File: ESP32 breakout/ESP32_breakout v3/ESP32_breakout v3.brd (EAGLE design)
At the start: 99.1 x 76.2 mm, 54 parts, among them J3 SCHA4B0419, Q3 BSS84, U1 ESP-WROOM-32, U2 NCP-1117223-3, U3 MCP2221ATSSOP14

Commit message: Layout and 80% routing done
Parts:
- removed R13: 10k, dr-library:RES-0603
- removed S1, S2: (no value), dr-library:SKHMQME010
- added BOOT, RST: (no value), dr-library:SKHMQME010
- added JP7, JP8: JUMPER_2-WAY, dr-library:1X02
- added R3: 10k, dr-library:RES-0603
- moved R12 83.8 mm to (7.62, 7.62), turned to 180 degrees
- moved R10 80.1 mm to (7.62, 10.2), turned to 180 degrees
- moved R9 80.1 mm to (11.4, 8.89), turned to 180 degrees
- moved C19 77.5 mm to (7.62, 12.7), turned to 180 degrees
- moved R14 76.3 mm to (7.62, 5.08), turned to 180 degrees
- moved R11 72.6 mm to (11.4, 11.4)
- moved J3 62.5 mm to (19.1, 22.9), turned to 270 degrees
- moved Q3 39.2 mm to (52.7, 29.2)
- moved R16 38.9 mm to (38.7, 29.2), turned to 270 degrees
- moved R8 37.6 mm to (57.1, 29.2), turned to 90 degrees
- moved R7 36.5 mm to (48.3, 29.2), turned to 270 degrees
- moved D7 36.4 mm to (38.7, 39.4), turned to 90 degrees
- moved R6 35.3 mm to (41.9, 29.2), turned to 270 degrees
- moved D5 32.4 mm to (41.9, 39.4), turned to 90 degrees
- moved R5 31.9 mm to (45.1, 29.2), turned to 270 degrees
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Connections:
- new net N$1: JP7.1, R9.1
- new net N$6: JP8.1, R3.1
- net +3V3: now also JP7.2, JP8.2; no longer R13.1, R9.1
- net CLK: no longer J3.5, R12.2
- net CMD: no longer J3.3, R11.2
- net EN: now also RST.3, RST.4; no longer S1.3, S1.4
- net GND: now also BOOT.1, BOOT.2, RST.1, RST.2; no longer S1.1, S1.2, S2.1, S2.2
- net IO0/T1: now also BOOT.3, BOOT.4; no longer S2.3, S2.4
- net IO12/T5: now also J3.1, R9.2
- net IO13/T4: now also J3.2, R10.2
- net IO14/T6: now also J3.5, R12.2
- net IO15/T3: now also J3.3, R11.2
- net IO2/T2: now also J3.7, R3.2
- net IO4/T0: now also J3.8, R14.2
- net SD0: no longer J3.7, R13.2
- net SD1: no longer J3.8, R14.2
- net SD2: no longer J3.1, R9.2
- net SD3: no longer J3.2, R10.2
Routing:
- net IO12/T5: track 0.00 -> 181.3 mm, vias 0 -> 5
- net IO14/T6: track 0.00 -> 180.7 mm, vias 0 -> 3
- net IO2/T2: track 0.00 -> 178.0 mm, vias 0 -> 3
- net IO15/T3: track 0.00 -> 153.0 mm, vias 0 -> 3
- net IO4/T0: track 0.00 -> 149.3 mm
- net IO13/T4: track 0.00 -> 140.4 mm, vias 0 -> 3
- net EN: track 0.00 -> 105.6 mm, vias 0 -> 1
- net IO0/T1: track 0.00 -> 102.0 mm, vias 0 -> 1
- net S_VP: track 0.00 -> 82.4 mm, vias 0 -> 1
- net S_VN: track 0.00 -> 80.0 mm, vias 0 -> 1
- net IO34: track 0.00 -> 72.2 mm, vias 0 -> 1
- net IO27/T7: track 0.00 -> 70.6 mm, vias 0 -> 1
- net IO35: track 0.00 -> 70.2 mm, vias 0 -> 1
- net IO19: track 0.00 -> 63.4 mm, vias 0 -> 2
- net +3V3: track 0.00 -> 63.2 mm, vias 0 -> 3
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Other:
- board size 99.1 x 76.2 mm -> 95.2 x 76.2 mm
- board text added: "NOTES Buttons further apart microSD should be more isolated microSD pinout HS2_CMD - io15 HS2_CLK - io14 HS2_D0 - io2 HS2_D1 - io4 HS2_D2 - io12 HS2_D3 - io13"

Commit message: v3 routing
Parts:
- added JP10, JP9: M02LONG, dr-library:1X02-LONG
- moved JP5 2.84 mm to (47.0, 5.08), turned to 270 degrees
- moved JP4 1.80 mm to (35.6, 5.08), turned to 270 degrees
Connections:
- net +3V3: now also JP10.2
- net GND: now also JP10.1, JP9.1
- net VCC: now also JP9.2
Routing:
- net +3V3: track 63.2 -> 389.0 mm, vias 3 -> 7
- net GND: track 26.6 -> 166.9 mm, vias 0 -> 54
- net VCC: track 0.00 -> 100.4 mm, vias 0 -> 1
- net IO0/T1: track 102.0 -> 160.0 mm, vias 1 -> 3
- net RX: track 17.9 -> 75.5 mm, vias 0 -> 3
- net TX: track 13.6 -> 68.9 mm, vias 0 -> 3
- net EN: track 105.6 -> 139.5 mm, vias 1 -> 2
- net N$3: track 0.00 -> 16.1 mm, vias 0 -> 2
- net N$2: track 0.00 -> 6.56 mm
- net IO12/T5: track 181.3 -> 180.2 mm
- net USBCFG: track 48.9 -> 48.1 mm
- added copper zone on layer 1, net +3V3
- added copper zone on layer 1, net GND
- added copper zone on layer 16, net GND
- added copper zone on layer 1, net VCC

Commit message: Finished tracing part 2
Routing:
- net SD1: track 23.2 -> 22.3 mm
- net SD3: track 28.3 -> 27.4 mm
- net CMD: track 30.1 -> 29.2 mm
- net SD0: track 27.5 -> 26.6 mm
- net CLK: track 25.7 -> 24.8 mm
- net +3V3: vias 7 -> 8
- net VCC: vias 1 -> 2
- net GND: vias 54 -> 121
- added copper zone on layer 16, net +3V3
- added copper zone on layer 16, net VCC

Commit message: PCB made
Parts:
- removed D7: (no value), dr-library:LED-1206
- removed R16: 330, dr-library:RES-0603
- added D1: VS-10BQ030-M3, dr-library:DO-214AA
- added R13: 10k, dr-library:RES-0603
- D2: value VS-10BQ030-M3 -> (none); device dr-library:DO-214AA -> dr-library:LED-1206
- JP10, JP9: value M02LONG -> JUMPER_3-WAY; device dr-library:1X02-LONG -> dr-library:1X03
- JP6, JP7: value JUMPER_2-WAY -> M02LONG; device dr-library:1X02 -> dr-library:1X02-LONG
- R9: value 10k -> 330
- moved R3 71.3 mm to (80.6, 23.5), turned to 0 degrees
- moved R15 71.2 mm to (11.4, 6.35), turned to 180 degrees
- moved JP8 51.2 mm to (63.5, 27.9)
- moved R9 42.1 mm to (48.3, 29.2), turned to 270 degrees
- moved JP6 36.1 mm to (35.6, 5.08), turned to 90 degrees
- moved JP7 31.4 mm to (47.0, 5.08), turned to 90 degrees
- moved JP10 30.9 mm to (20.3, 10.2)
- moved JP9 24.7 mm to (15.2, 10.2)
- moved D2 20.3 mm to (35.6, 39.4), turned to 90 degrees
- moved D3 9.52 mm to (45.1, 39.4)
- moved R7 9.52 mm to (38.7, 29.2)
- moved R14 5.39 mm to (11.4, 8.89)
- moved JP4 3.81 mm to (39.4, 5.08), turned to 90 degrees
- moved JP5 3.81 mm to (50.8, 5.08), turned to 90 degrees
- moved D4 3.18 mm to (41.9, 39.4)
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- renumbered C18 to C8, C19 to C9, RST to RESET
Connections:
- removed net N$1: JP7.1, R9.1
- new net N$7: JP10.1, R15.1
- net +3V3: now also JP9.2, R13.1; no longer JP8.2, R14.1
- net GND: now also D2.C, JP6.1, JP7.1; no longer D7.C, JP10.1, JP9.1
- net HEART: now also JP8.1; no longer JP6.1
- net IO12/T5: now also R14.2; no longer R9.2
- net IO19: now also JP8.2; no longer JP6.2
- net IO2/T2: now also R15.2; no longer R3.2
- net IO4/T0: now also R13.2; no longer R14.2
- net N$10: now also R9.2; no longer R7.2
- net N$11: now also D4.A; no longer D5.A
- net N$2: now also D1.A; no longer D2.A
- net N$3: now also R3.1; no longer R15.1
- net N$4: now also D5.A, R7.1; no longer D7.A, R16.1
- net N$5: now also D2.A; no longer D3.A
- net N$6: now also JP9.1, R14.1; no longer JP8.1, R3.1
- net N$8: now also D3.A; no longer D4.A
- net N$9: now also R9.1; no longer R7.1
- net USBCFG: now also R7.2; no longer R16.2
- net VCC: now also D1.C, JP6.2; no longer D2.C, JP9.2
- net V_MCP: now also R3.2; no longer R15.2
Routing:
- net +3V3: track 389.0 -> 372.5 mm, vias 8 -> 23
- net N$7: track 0.00 -> 10.2 mm
- net N$1: track 6.09 -> 0.00 mm
- net GND: track 166.9 -> 163.1 mm, vias 121 -> 176
- net VCC: track 100.4 -> 97.5 mm, vias 2 -> 19
- net TX: track 68.9 -> 66.8 mm
- net RX: track 75.5 -> 73.3 mm
- net IO0/T1: track 160.0 -> 157.8 mm
- net IO19: track 63.4 -> 61.6 mm
- net SD1: track 22.3 -> 21.0 mm
- net CLK: track 24.8 -> 23.6 mm
- net S_VP: track 82.0 -> 80.7 mm
- net SD3: track 27.4 -> 26.1 mm
- net IO35: track 69.8 -> 68.5 mm
- net IO34: track 71.8 -> 70.6 mm
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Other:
- outline, holes or cut-outs redrawn
- board text added: "3.3V"
- board text added: "5V"
- board text added: "CLK"
- board text added: "CMD"
- board text added: "EN"
- board text added: "ESP32 Breakout D. Rances 10 Sep 2017 v3"
- board text added: "ESP32 Breakout and Development Board"
- board text added: "GND"
- board text added: "HEART"
- board text added: "HEART/IO19"
- board text added: "IO0"
- board text added: "IO12"
- board text added: "IO13"
- board text added: "IO14"
- board text added: "IO15"
- board text added: "IO16"
- board text added: "IO17"
- board text added: "IO18"
- board text added: "IO19"
- board text added: "IO2"
- board text added: "IO21"
- board text added: "IO22"
- board text added: "IO23"
- board text added: "IO25"
- board text added: "IO26"
- board text added: "IO27"
- board text added: "IO34"
- board text added: "IO35"
- board text added: "IO4"
- board text added: "IO5"
- board text added: "Pullups for DAT0 and DAT2 of microSD. Keep disabled to flash the ESP32"
- board text added: "RX"
- board text added: "Remove header to disconnect HEART LED and IO19"
- board text added: "SD0"
- board text added: "SD1"
- board text added: "SD2"
- board text added: "SD3"
- board text added: "SVN"
- board text added: "SVP"
- board text added: "Switch to enable USB-UART flashing and debugging"
- board text added: "T0"
- board text added: "T0/IO4"
- board text added: "T1"
- board text added: "T1/IO0"
- board text added: "T2"
- board text added: "T2/IO2"
- board text added: "T3"
- board text added: "T3/IO15"
- board text added: "T4"
- board text added: "T4/IO13"
- board text added: "T5"
- board text added: "T5/IO12"
- board text added: "T6"
- board text added: "T6/IO14"
- board text added: "T7"
- board text added: "T7/IO27"
- board text added: "TX"
- board text added: "USBCFG"
- board text added: "pullups disabled"
- board text added: "pullups enabled"
- board text removed: "NOTES Buttons further apart microSD should be more isolated microSD pinout HS2_CMD - io15 HS2_CLK - io14 HS2_D0 - io2 HS2_D1 - io4 HS2_D2 - io12 HS2_D3 - io13"

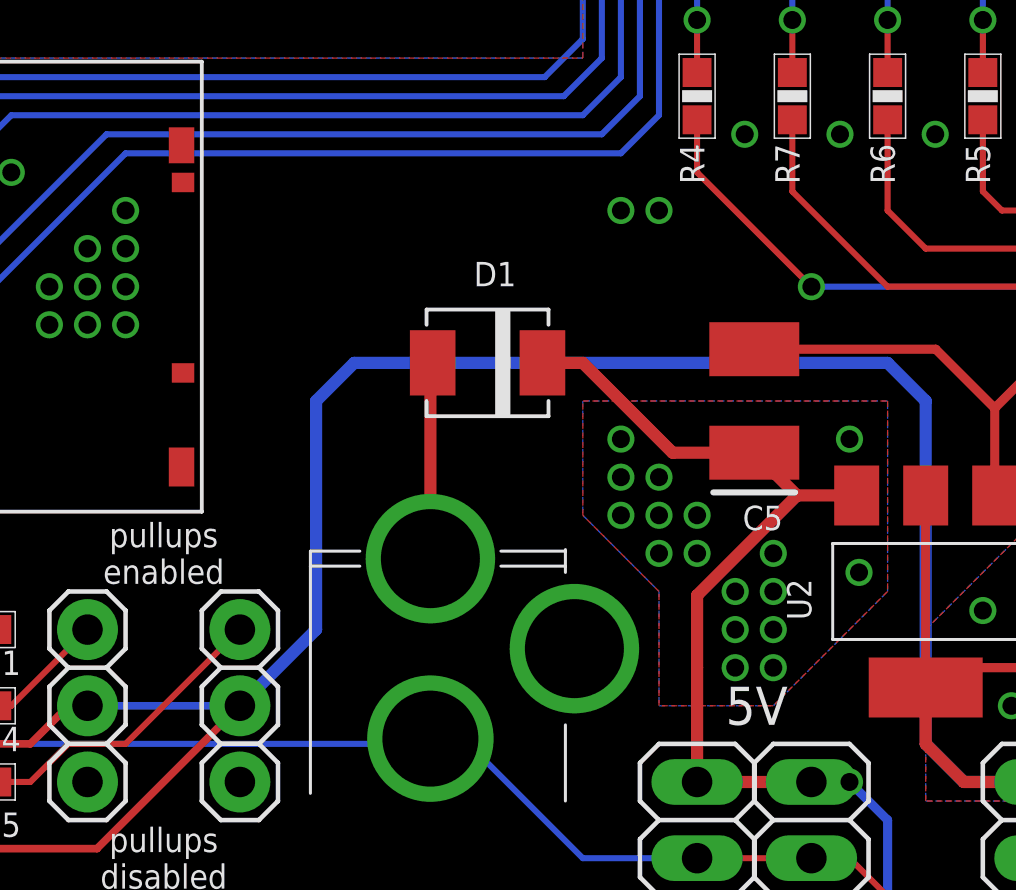
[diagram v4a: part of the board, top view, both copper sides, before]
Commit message: Added LED for microSD CD
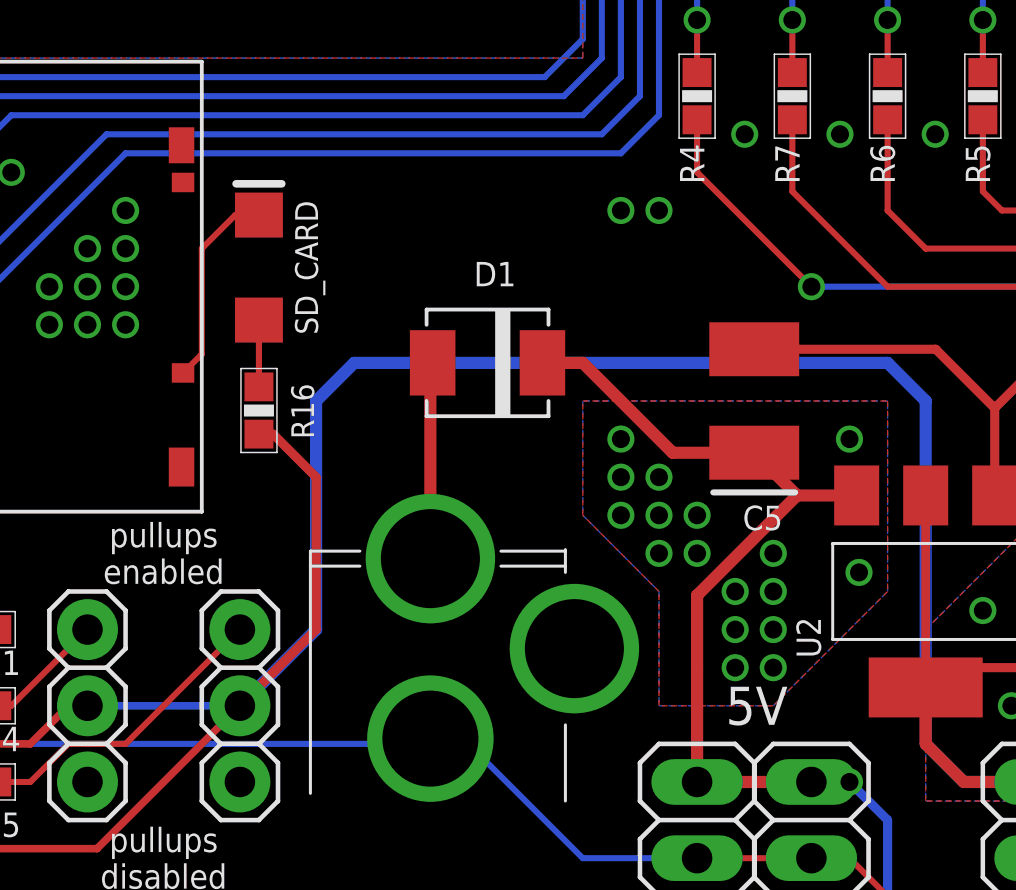
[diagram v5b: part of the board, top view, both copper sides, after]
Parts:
- added D7: (no value), dr-library:LED-1206
- added R16: 330, dr-library:RES-0603
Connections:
- new net N$12: D7.C, J3.CD
- new net N$14: D7.A, R16.2
- net +3V3: now also R16.1
- net GND: now also J3.COMMON
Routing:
- net +3V3: track 372.5 -> 383.7 mm
- net N$12: track 0.00 -> 6.77 mm
- net N$14: track 0.00 -> 2.23 mm
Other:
- board text added: "SD_CARD"
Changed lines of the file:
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@@
 Keep disabled to flash
 the ESP32</text>
+<text x="22.5425" y="23.495" size="0.762" layer="21" font="vector" ratio="20" rot="R90" align="center">SD_CARD</text>
 </plain>
 <attributes>
@@
 </element>
 <element name="U2" library="dr-library" package="SOT-223-3" value="NCP-1117223-3" x="43.18" y="12.7" smashed="yes" rot="R180">
-<attribute name="NAME" x="39.37" y="11.7475" size="0.8128" layer="21" font="vector" ratio="20" rot="R90"/>
+<attribute name="NAME" x="39.6875" y="10.4775" size="0.8128" layer="21" font="vector" ratio="20" rot="R90"/>
 </element>
 <element name="U3" library="dr-library" package="TSSOP-14" value="MCP2221ATSSOP14" x="82.55" y="19.05" smashed="yes" rot="R90">
@@
 <element name="JP9" library="dr-library" package="1X03" value="JUMPER_3-WAY" x="15.24" y="10.16" smashed="yes" rot="R270"/>
 <element name="JP10" library="dr-library" package="1X03" value="JUMPER_3-WAY" x="20.32" y="10.16" smashed="yes" rot="R270"/>
+<element name="R16" library="dr-library" package="RES-0603" value="330" x="20.955" y="18.7325" smashed="yes" rot="R90">
+<attribute name="NAME" x="22.795" y="17.7825" size="0.762" layer="25" font="vector" ratio="20" rot="R90"/>
+</element>
+<element name="D7" library="dr-library" package="LED-1206" value="" x="20.955" y="23.495" smashed="yes" rot="R90">
+<attribute name="VALUE" x="22.86" y="20.955" size="0.762" layer="27" font="vector" ratio="20" rot="R90"/>
+</element>
 </elements>
 <signals>
@@
 <wire x1="25.4" y1="7.62" x2="11.43" y2="7.62" width="0.2032" layer="16"/>
 <wire x1="11.43" y1="7.62" x2="6.731" y2="12.319" width="0.2032" layer="16"/>
+<contactref element="J3" pad="COMMON"/>
 </signal>
 <signal name="+3V3">
@@
 <wire x1="15.5575" y1="4.1275" x2="9.36" y2="4.1275" width="0.254" layer="1"/>
 <wire x1="9.36" y1="4.1275" x2="8.4075" y2="5.08" width="0.254" layer="1"/>
+<contactref element="R16" pad="1"/>
+<wire x1="20.955" y1="17.945" x2="21.425" y2="17.945" width="0.3048" layer="1"/>
+<wire x1="21.425" y1="17.945" x2="22.86" y2="16.51" width="0.3048" layer="1"/>
+<wire x1="22.86" y1="16.51" x2="22.86" y2="11.43" width="0.3048" layer="1"/>
+<wire x1="22.86" y1="11.43" x2="20.32" y2="8.89" width="0.3048" layer="1"/>
 </signal>
 <signal name="EN">
@@
 <wire x1="13.335" y1="6.35" x2="12.2175" y2="6.35" width="0.2032" layer="1"/>
 </signal>
+<signal name="N$12">
+<contactref element="J3" pad="CD"/>
+<contactref element="D7" pad="C"/>
+<wire x1="20.955" y1="25.245" x2="20.165" y2="25.245" width="0.2032" layer="1"/>
+<wire x1="20.165" y1="25.245" x2="19.05" y2="24.13" width="0.2032" layer="1"/>
+<wire x1="19.05" y1="24.13" x2="19.05" y2="20.61" width="0.2032" layer="1"/>
+<wire x1="19.05" y1="20.61" x2="18.425" y2="19.985" width="0.2032" layer="1"/>
+</signal>
+<signal name="N$14">
+<contactref element="R16" pad="2"/>
+<contactref element="D7" pad="A"/>
+<wire x1="20.955" y1="19.52" x2="20.955" y2="21.745" width="0.2032" layer="1"/>
+</signal>
 </signals>
